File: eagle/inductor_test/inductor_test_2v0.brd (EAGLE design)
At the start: 25.4 x 25.4 mm, 23 parts, among them J1 MA02-1_ROUND

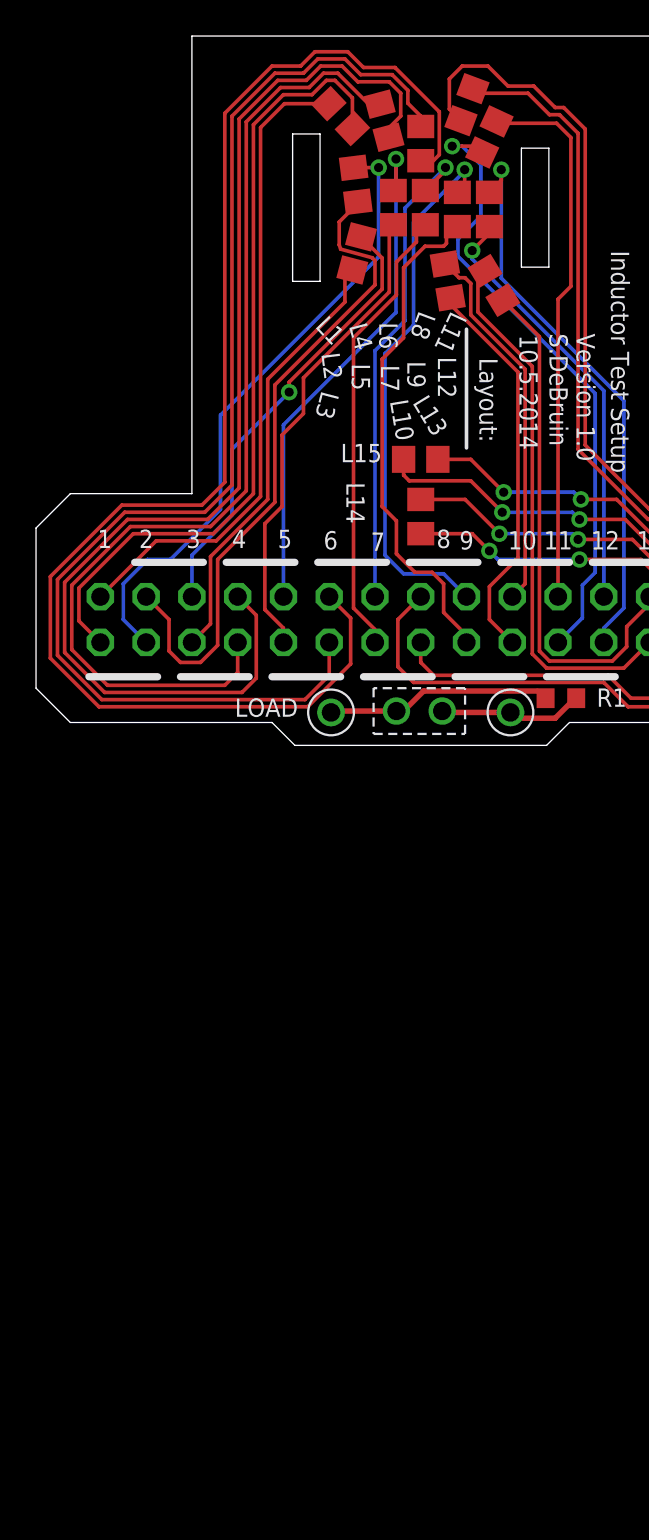
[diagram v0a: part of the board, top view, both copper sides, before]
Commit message: added new amplifiers for inductor inspector
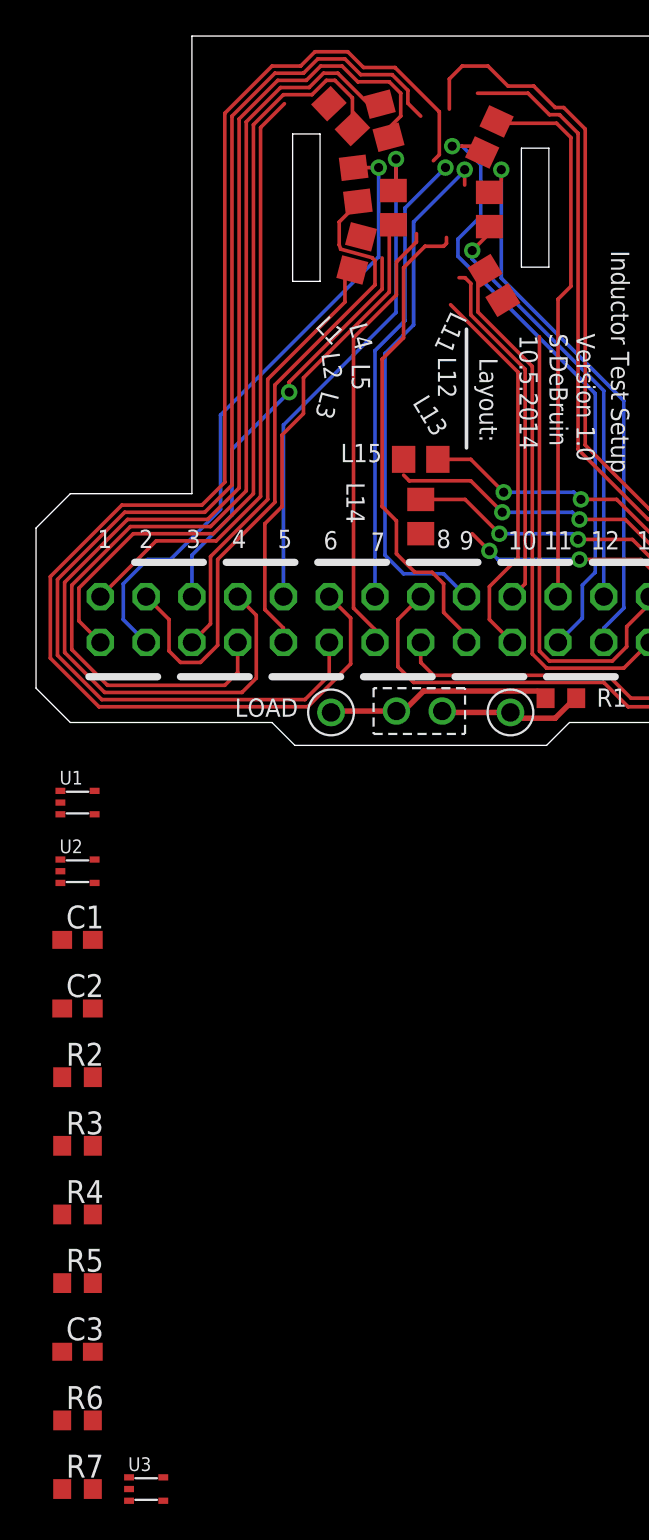
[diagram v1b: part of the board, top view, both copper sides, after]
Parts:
- removed L10, L6, L7, L8, L9: (no value), rcl:L0805
- added C1, C2, C3: (no value), rcl:C0603
- added R2, R3, R4, R5, R6, R7: (no value), rcl:R0603
- added U1: MCP6V3, powerfilm:SC70-5
- added U2, U3: OPA333, powerfilm:SC70-5
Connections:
- new net +3V3: C1.1, C2.1, C3.1, U1.P5, U2.P5, U3.P5
- new net GND: C1.2, C2.2, C3.2, R4.1, R5.1, R7.1, U1.P2, U2.P2, U3.P2
- new net L_SIG: U1.P1, U2.P1, U3.P1
- new net N$3: R6.1, R7.2, U3.P3
- new net N$4: R2.1, R4.2, U1.P3
- new net N$6: R3.1, R5.2, U2.P3
- new net OUT_MCP6V3: R2.2, U1.P4
- new net OUT_OPA333: R3.2, R6.2, U2.P4, U3.P4
- net C1P1: no longer L14.1
- net C2P1: no longer L15.1
- net L10P1: no longer L10.1
- net L10P2: no longer L10.2
- net L11P1: now also L1.1, L12.1, L13.1, L14.1, L15.1, L2.1, L3.1, L4.1, L5.1
- net L12P1: no longer L12.1
- net L13P1: no longer L13.1
- net L1P1: no longer L1.1
- net L2P1: no longer L2.1
- net L3P1: no longer L3.1
- net L4P1: no longer L4.1
- net L5P1: no longer L5.1
- net L6P1: no longer L6.1
- net L6P2: no longer L6.2
- net L7P1: no longer L7.1
- net L7P2: no longer L7.2
- net L8P1: no longer L8.1
- net L8P2: no longer L8.2
- net L9P1: no longer L9.1
- net L9P2: no longer L9.2
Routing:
- net L13P1: track 29.0 -> 26.2 mm
- net C1P1: track 18.7 -> 15.8 mm
- net L1P1: track 36.0 -> 33.5 mm
- net L3P1: track 24.8 -> 23.2 mm
- net L7P1: track 27.2 -> 25.6 mm
- net L10P2: track 20.8 -> 19.7 mm
- net L12P1: track 31.0 -> 30.1 mm
- net L8P2: track 78.9 -> 77.9 mm
- net C2P1: track 24.4 -> 23.6 mm
- net L9P2: track 27.9 -> 27.1 mm
- net L6P2: track 78.1 -> 77.4 mm
- net L7P2: track 25.3 -> 24.6 mm
- net L4P1: track 57.1 -> 56.5 mm
- net L9P1: track 30.1 -> 29.6 mm
- net L6P1: track 69.1 -> 68.6 mm

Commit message: more work in inductor board
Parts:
- added C4, C5, C6, C7, C8: (no value), rcl:C0603
- added R10, R11, R8, R9: (no value), rcl:R0603
- added U4, U6: MAX4238, powerfilm:SOT-23-6
- added U5: LMP2014, powerfilm:TSSOP-14
- added U7: OPA376, powerfilm:SC70-5
- U3: value OPA333 -> OPA376
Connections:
- new net N$5: R8.2, R9.1, U4.P4
- new net N$7: C8.2, U7.P1
- new net N$8: R10.1, R11.2, U5.P2
- new net N$9: C6.2, U6.P3
- new net OUT1_LMP2014: R10.2, U5.P1
- new net OUT1_MAX4238: C6.1, R9.2, U4.P1
- new net OUT1_OPA376: C8.1, R6.2, U3.P4
- net +3V3: now also C4.1, C5.1, U4.P5, U4.P6, U5.P4
- net GND: now also C4.2, C5.2, R11.1, R8.1, U4.P2, U5.P11
- net L_SIG: now also U4.P3
- net OUT_OPA333: no longer R6.2, U3.P4
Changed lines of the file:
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@@
 <?xml version="1.0" encoding="utf-8"?>
 <!DOCTYPE eagle SYSTEM "eagle.dtd">
-<eagle version="6.5.0">
+<eagle version="6.3">
 <drawing>
 <settings>
@@
 </element>
 <element name="U2" library="powerfilm" package="SC70-5" value="OPA333" x="-19.05" y="-36.83">
-<attribute name="DIGIKEY" value="MCP6V31UT-E/LTCT-ND" x="-19.05" y="-36.83" size="1.778" layer="27" display="off"/>
+<attribute name="DIGIKEY" value="296-19547-1-ND" x="-19.05" y="-36.83" size="1.778" layer="27" display="off"/>
 </element>
 <element name="C1" library="rcl" package="C0603" value="" x="-19.05" y="-40.64"/>
@@
 <element name="R4" library="rcl" package="R0603" value="" x="-19.05" y="-55.88"/>
 <element name="R5" library="rcl" package="R0603" value="" x="-19.05" y="-59.69"/>
-<element name="U3" library="powerfilm" package="SC70-5" value="OPA333" x="-15.24" y="-71.12">
-<attribute name="DIGIKEY" value="MCP6V31UT-E/LTCT-ND" x="-19.05" y="-63.5" size="1.778" layer="27" display="off"/>
+<element name="U3" library="powerfilm" package="SC70-5" value="OPA376" x="-15.24" y="-71.12">
+<attribute name="DIGIKEY" value="296-22191-1-ND" x="-19.05" y="-63.5" size="1.778" layer="27" display="off"/>
 </element>
 <element name="C3" library="rcl" package="C0603" value="" x="-19.05" y="-63.5"/>
 <element name="R6" library="rcl" package="R0603" value="" x="-19.05" y="-67.31"/>
 <element name="R7" library="rcl" package="R0603" value="" x="-19.05" y="-71.12"/>
+<element name="U4" library="powerfilm" package="SOT-23-6" value="MAX4238" x="-24.13" y="-69.85">
+<attribute name="DIGIKEY" value="MAX4238AUT+TCT-ND" x="-24.13" y="-69.85" size="1.778" layer="27" display="off"/>
+</element>
+<element name="C4" library="rcl" package="C0603" value="" x="-24.13" y="-74.93"/>
+<element name="R8" library="rcl" package="R0603" value="" x="-24.13" y="-78.74"/>
+<element name="R9" library="rcl" package="R0603" value="" x="-24.13" y="-82.55"/>
+<element name="C5" library="rcl" package="C0603" value="" x="-24.13" y="-86.36"/>
+<element name="U5" library="powerfilm" package="TSSOP-14" value="LMP2014" x="-21.59" y="-92.71">
+<attribute name="DIGIKEY" value="LMP2014MT/NOPB-ND" x="-21.59" y="-92.71" size="1.778" layer="27" display="off"/>
+</element>
+<element name="U6" library="powerfilm" package="SOT-23-6" value="MAX4238" x="-29.21" y="-92.71">
+<attribute name="DIGIKEY" value="MAX4238AUT+TCT-ND" x="-29.21" y="-92.71" size="1.778" layer="27" display="off"/>
+</element>
+<element name="U7" library="powerfilm" package="SC70-5" value="OPA376" x="-29.21" y="-97.79">
+<attribute name="DIGIKEY" value="296-22191-1-ND" x="-29.21" y="-97.79" size="1.778" layer="27" display="off"/>
+</element>
+<element name="R10" library="rcl" package="R0603" value="" x="-29.21" y="-101.6"/>
+<element name="R11" library="rcl" package="R0603" value="" x="-29.21" y="-105.41"/>
+<element name="C6" library="rcl" package="C0603" value="" x="-29.21" y="-109.22"/>
+<element name="C7" library="rcl" package="C0603" value="" x="-29.21" y="-113.03"/>
+<element name="C8" library="rcl" package="C0603" value="" x="-29.21" y="-116.84"/>
 </elements>
 <signals>
@@
 <contactref element="C3" pad="1"/>
 <contactref element="U3" pad="P5"/>
-<wire x1="-14.29" y1="-70.47" x2="-19.9" y2="-63.5" width="0" layer="19" extent="1-1"/>
+<contactref element="U4" pad="P5"/>
+<contactref element="U4" pad="P6"/>
+<contactref element="C4" pad="1"/>
+<contactref element="U5" pad="P4"/>
+<contactref element="C5" pad="1"/>
+<wire x1="-24.98" y1="-86.36" x2="-24.49" y2="-92.71" width="0" layer="19" extent="1-1"/>
+<wire x1="-24.98" y1="-74.93" x2="-24.98" y2="-86.36" width="0" layer="19" extent="1-1"/>
+<wire x1="-22.93" y1="-69.85" x2="-24.98" y2="-74.93" width="0" layer="19" extent="1-1"/>
+<wire x1="-22.93" y1="-68.9" x2="-22.93" y2="-69.85" width="0" layer="19" extent="1-1"/>
+<wire x1="-19.9" y1="-63.5" x2="-22.93" y2="-68.9" width="0" layer="19" extent="1-1"/>
+<wire x1="-14.29" y1="-70.47" x2="-22.93" y2="-69.85" width="0" layer="19" extent="1-1"/>
 <wire x1="-19.9" y1="-44.45" x2="-19.9" y2="-63.5" width="0" layer="19" extent="1-1"/>
 <wire x1="-19.9" y1="-40.64" x2="-19.9" y2="-44.45" width="0" layer="19" extent="1-1"/>
@@
 <contactref element="C3" pad="2"/>
 <contactref element="R7" pad="1"/>
+<contactref element="R8" pad="1"/>
+<contactref element="U4" pad="P2"/>
+<contactref element="C4" pad="2"/>
+<contactref element="C5" pad="2"/>
+<contactref element="U5" pad="P11"/>
+<contactref element="R11" pad="1"/>
+<wire x1="-18.69" y1="-92.71" x2="-30.06" y2="-105.41" width="0" layer="19" extent="1-1"/>
+<wire x1="-23.28" y1="-86.36" x2="-18.69" y2="-92.71" width="0" layer="19" extent="1-1"/>
+<wire x1="-24.98" y1="-78.74" x2="-23.28" y2="-86.36" width="0" layer="19" extent="1-1"/>
+<wire x1="-23.28" y1="-74.93" x2="-24.98" y2="-78.74" width="0" layer="19" extent="1-1"/>
+<wire x1="-19.9" y1="-71.12" x2="-23.28" y2="-74.93" width="0" layer="19" extent="1-1"/>
 <wire x1="-16.19" y1="-71.12" x2="-19.9" y2="-71.12" width="0" layer="19" extent="1-1"/>
+<wire x1="-25.33" y1="-69.85" x2="-23.28" y2="-74.93" width="0" layer="19" extent="1-1"/>
 <wire x1="-18.2" y1="-63.5" x2="-19.9" y2="-71.12" width="0" layer="19" extent="1-1"/>
 <wire x1="-19.9" y1="-59.69" x2="-18.2" y2="-63.5" width="0" layer="19" extent="1-1"/>
@@
 <contactref element="U2" pad="P4"/>
 <contactref element="R3" pad="2"/>
-<contactref element="U3" pad="P4"/>
-<contactref element="R6" pad="2"/>
-<wire x1="-18.2" y1="-67.31" x2="-14.29" y2="-71.77" width="0" layer="19" extent="1-1"/>
-<wire x1="-18.2" y1="-52.07" x2="-18.2" y2="-67.31" width="0" layer="19" extent="1-1"/>
 <wire x1="-18.1" y1="-37.48" x2="-18.2" y2="-52.07" width="0" layer="19" extent="1-1"/>
 </signal>
@@
 <contactref element="U2" pad="P1"/>
 <contactref element="U3" pad="P1"/>
+<contactref element="U4" pad="P3"/>
+<wire x1="-16.19" y1="-70.47" x2="-25.33" y2="-70.8" width="0" layer="19" extent="1-1"/>
 <wire x1="-20" y1="-36.18" x2="-16.19" y2="-70.47" width="0" layer="19" extent="1-1"/>
 <wire x1="-20" y1="-32.37" x2="-20" y2="-36.18" width="0" layer="19" extent="1-1"/>
@@
 <wire x1="-19.9" y1="-67.31" x2="-18.2" y2="-71.12" width="0" layer="19" extent="1-1"/>
 </signal>
+<signal name="OUT1_OPA376">
+<contactref element="U3" pad="P4"/>
+<contactref element="R6" pad="2"/>
+<contactref element="C8" pad="1"/>
+<wire x1="-14.29" y1="-71.77" x2="-30.06" y2="-116.84" width="0" layer="19" extent="1-1"/>
+<wire x1="-18.2" y1="-67.31" x2="-14.29" y2="-71.77" width="0" layer="19" extent="1-1"/>
+</signal>
+<signal name="N$5">
+<contactref element="U4" pad="P4"/>
+<contactref element="R8" pad="2"/>
+<contactref element="R9" pad="1"/>
+<wire x1="-23.28" y1="-78.74" x2="-24.98" y2="-82.55" width="0" layer="19" extent="1-1"/>
+<wire x1="-22.93" y1="-70.8" x2="-23.28" y2="-78.74" width="0" layer="19" extent="1-1"/>
+</signal>
+<signal name="OUT1_MAX4238">
+<contactref element="U4" pad="P1"/>
+<contactref element="R9" pad="2"/>
+<contactref element="C6" pad="1"/>
+<wire x1="-23.28" y1="-82.55" x2="-30.06" y2="-109.22" width="0" layer="19" extent="1-1"/>
+<wire x1="-25.33" y1="-68.9" x2="-23.28" y2="-82.55" width="0" layer="19" extent="1-1"/>
+</signal>
+<signal name="OUT1_LMP2014">
+<contactref element="U5" pad="P1"/>
+<contactref element="R10" pad="2"/>
+<wire x1="-24.49" y1="-90.76" x2="-28.36" y2="-101.6" width="0" layer="19" extent="1-1"/>
+</signal>
+<signal name="N$8">
+<contactref element="U5" pad="P2"/>
+<contactref element="R10" pad="1"/>
+<contactref element="R11" pad="2"/>
+<wire x1="-30.06" y1="-101.6" x2="-28.36" y2="-105.41" width="0" layer="19" extent="1-1"/>
+<wire x1="-24.49" y1="-91.41" x2="-30.06" y2="-101.6" width="0" layer="19" extent="1-1"/>
+</signal>
+<signal name="N$7">
+<contactref element="C8" pad="2"/>
+<contactref element="U7" pad="P1"/>
+<wire x1="-30.16" y1="-97.14" x2="-28.36" y2="-116.84" width="0" layer="19" extent="1-1"/>
+</signal>
+<signal name="N$9">
+<contactref element="C6" pad="2"/>
+<contactref element="U6" pad="P3"/>
+<wire x1="-30.41" y1="-93.66" x2="-28.36" y2="-109.22" width="0" layer="19" extent="1-1"/>
+</signal>
 </signals>

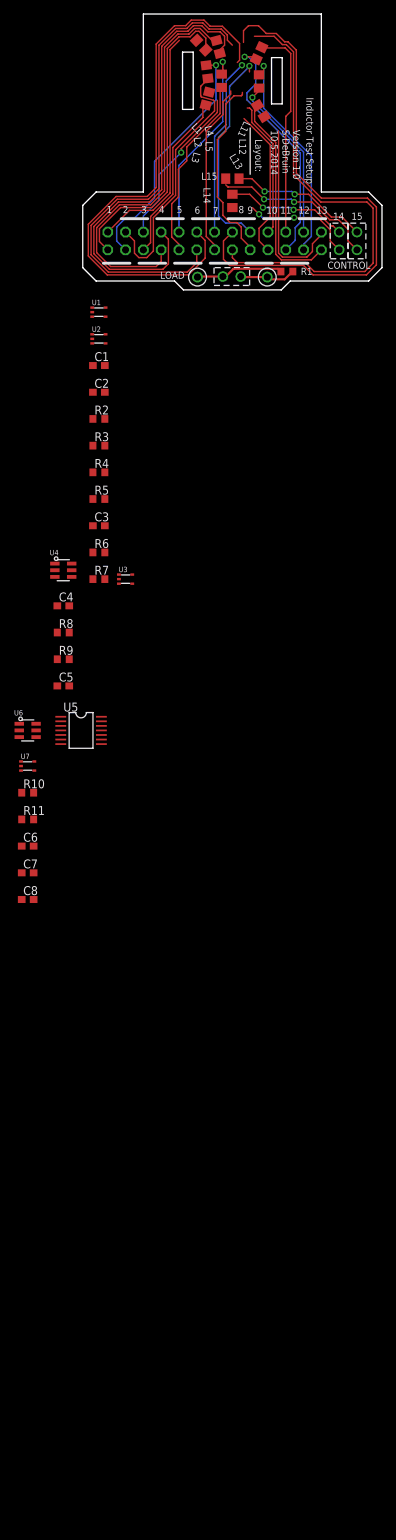
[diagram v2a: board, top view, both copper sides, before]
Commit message: added new amplifier configuration
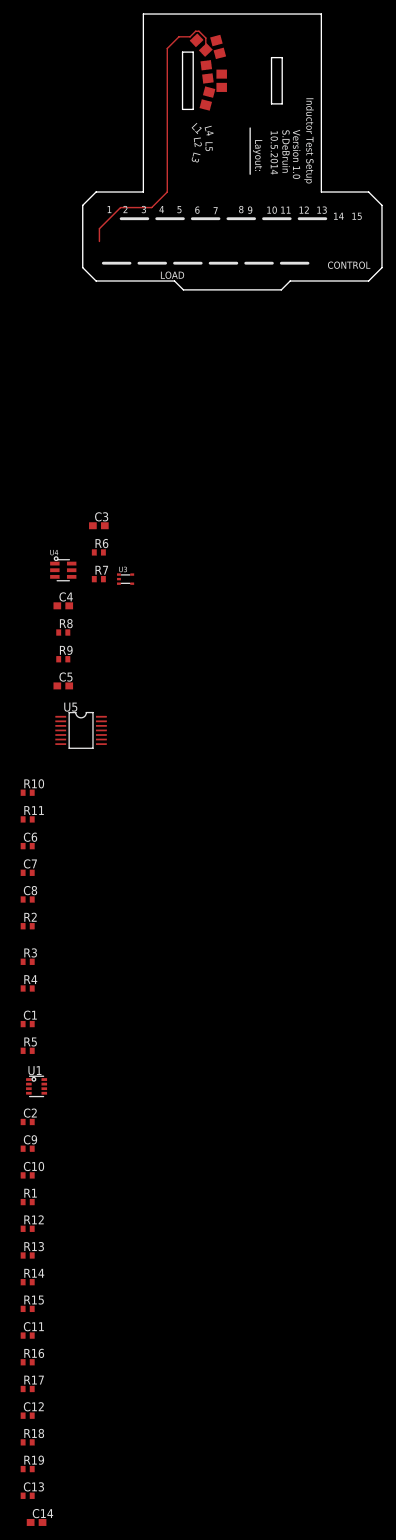
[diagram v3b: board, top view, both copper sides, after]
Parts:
- removed J1, SV2, SV3: MA02-1_ROUND, con-lstb:MA02-1_ROUND
- removed L11, L12, L13, L14, L15: (no value), rcl:L0805
- removed SV1: (no value), con-lstb:MA13-2_BARE
- removed TP1, TP2: TP_STD, skyspecs:TP
- removed U2: OPA333, powerfilm:SC70-5
- removed U6: MAX4238, powerfilm:SOT-23-6
- removed U7: OPA376, powerfilm:SC70-5
- added C10, C11, C12, C13, C9: (no value), rcl:C0402
- added C14: (no value), rcl:C0603
- added R12, R13, R14, R15, R16, R17, R18, R19: (no value), rcl:R0402
- C1, C2, C6, C7, C8: device rcl:C0603 -> rcl:C0402
- R1, R10, R11, R5, R6, R7, R8, R9: device rcl:R0603 -> rcl:R0402
- R2: value (none) -> 200; device rcl:R0603 -> rcl:R0402
- R3: value (none) -> 1M; device rcl:R0603 -> rcl:R0402
- R4: value (none) -> 75; device rcl:R0603 -> rcl:R0402
- U1: value MCP6V3 -> OPA2369; device powerfilm:SC70-5 -> powerfilm:SOT-23-8
- U3: value OPA376 -> SC70
- U4: value MAX4238 -> SOT-23-6
- U5: value LMP2014 -> TSSOP-14
- moved R1 137.8 mm to (-29.2, -160.0), turned to 0 degrees
- moved U1 110.8 mm to (-27.9, -143.5)
- moved C2 104.6 mm to (-29.2, -148.6)
- moved C1 94.5 mm to (-29.2, -134.6)
- moved R5 79.4 mm to (-29.2, -138.4)
- moved R3 74.4 mm to (-29.2, -125.7)
- moved R4 74.4 mm to (-29.2, -129.5)
- moved R2 73.1 mm to (-29.2, -120.7)
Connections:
- net OUT1_MAX4238 renamed OUT1_SOT23
- net OUT1_OPA376 renamed OUT1_SC70
- removed net C1P1: SV2.1
- removed net C1P2: L14.2, SV2.2
- removed net C2P1: SV3.2
- removed net C2P2: L15.2, SV3.1
- removed net L10P1: SV1.8
- removed net L10P2: SV1.7
- removed net L11P1: L1.1, L11.1, L12.1, L13.1, L14.1, L15.1, L2.1, L3.1, L4.1, L5.1, SV1.5
- removed net L11P2: L11.2, SV1.6
- removed net L12P1: SV1.4
- removed net L12P2: L12.2, SV1.3
- removed net L13P1: SV1.1
- removed net L13P2: L13.2, SV1.2
- removed net L1P1: SV1.25
- removed net L2P1: SV1.24
- removed net L2P2: L2.2, SV1.23
- removed net L3P1: SV1.21
- removed net L3P2: L3.2, SV1.22
- removed net L4P1: SV1.20
- removed net L4P2: L4.2, SV1.19
- removed net L5P1: SV1.17
- removed net L5P2: L5.2, SV1.18
- removed net L6P1: SV1.16
- removed net L6P2: SV1.15
- removed net L7P1: SV1.13
- removed net L7P2: SV1.14
- removed net L8P1: SV1.12
- removed net L8P2: SV1.11
- removed net L9P1: SV1.9
- removed net L9P2: SV1.10
- removed net OUT1_LMP2014: R10.2, U5.P1
- removed net OUT_MCP6V3: R2.2, U1.P4
- removed net OUT_OPA333: R3.2, U2.P4
- new net N$10: C6.2, R12.1, U1.P5
- new net N$11: C11.1, R15.1
- new net N$12: C7.2, R13.1, U5.P5
- new net N$14: R16.1, R17.2, U1.P6
- new net N$15: C12.1, R17.1
- new net N$17: R18.1, R19.2, U5.P6
- new net N$18: C13.1, R19.1
- new net OUT1_TSSOP14: C7.1, R10.2, U5.P1
- new net OUT2_SC70: R14.2, U1.P1
- new net OUT2_SOT23: R16.2, U1.P7
- new net OUT2_TSSOP14: R18.2, U5.P7
- new net VREF_1V65: R5.2
- new net VREF_V054: R1.2, R12.2, R13.2
- net +3V3: now also C14.1, R3.1, U1.P8; no longer C1.1, C2.1, U1.P5, U2.P5
- net GND: now also C10.2, C11.2, C12.2, C13.2, C14.2, C9.2, U1.P4; no longer C1.2, R11.1, R5.1, R7.1, R8.1, U1.P2, U2.P2
- net L1P2: now also L2.2, L3.2, L4.2, L5.2, R2.1, R3.2, R4.2; no longer SV1.26
- net L_SIG: now also C1.2, R5.1, U5.P3; no longer U1.P1, U2.P1
- net N$1: now also C10.1, R11.1; no longer J1.2, R1.1, TP1.P$1
- net N$2: now also C9.1, R8.1; no longer J1.1, R1.2, TP2.P$1
- net N$4: now also C1.1, L1.1, L2.1, L3.1, L4.1, L5.1, R2.2; no longer R2.1, R4.2, U1.P3
- net N$6: now also C2.1, R7.1; no longer R3.1, R5.2, U2.P3
- net N$7: now also R1.1, U1.P3; no longer U7.P1
- net N$9: now also R14.1, R15.2, U1.P2; no longer C6.2, U6.P3
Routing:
- net L8P2: track 77.9 -> 0.00 mm
- net L6P2: track 77.4 -> 0.00 mm
- net L6P1: track 68.6 -> 0.00 mm
- net L8P1: track 67.7 -> 0.00 mm
- net L4P2: track 66.6 -> 0.00 mm
- net L4P1: track 56.5 -> 0.00 mm
- net L2P2: track 37.0 -> 0.00 mm
- net L11P2: track 34.9 -> 0.00 mm, vias 1 -> 0
- net L2P1: track 34.9 -> 0.00 mm, vias 1 -> 0
- net L1P1: track 33.5 -> 0.00 mm
- net L11P1: track 30.3 -> 0.00 mm
- net L12P1: track 30.1 -> 0.00 mm, vias 1 -> 0
- net L13P2: track 30.1 -> 0.00 mm
- net L9P1: track 29.6 -> 0.00 mm, vias 1 -> 0
- net L5P1: track 28.5 -> 0.00 mm, vias 1 -> 0
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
